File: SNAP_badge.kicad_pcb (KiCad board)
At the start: 2 copper layers, 63.5 x 127 mm, 149 parts, among them P1 MicroB, P2 CONN_01X08, P3 CONN_01X08, P4 CONN_01X10, P5 CONN_01X06, P6 CONN_02X03, Q1 ZXMN2F30FHCT-ND, Q2 Si2305DS, SW1 SWITCH_DPDT, SW2 SW_PUSH, SW3 SW_PUSH, SW4 SW_PUSH, SW5 SW_DIP_8, U1 SM220, U2 AS1115, U3 FT230XS, U4 LD1117S33CTR, U5 LIS3DH, U6 TPS61070, U7 NLSX4373

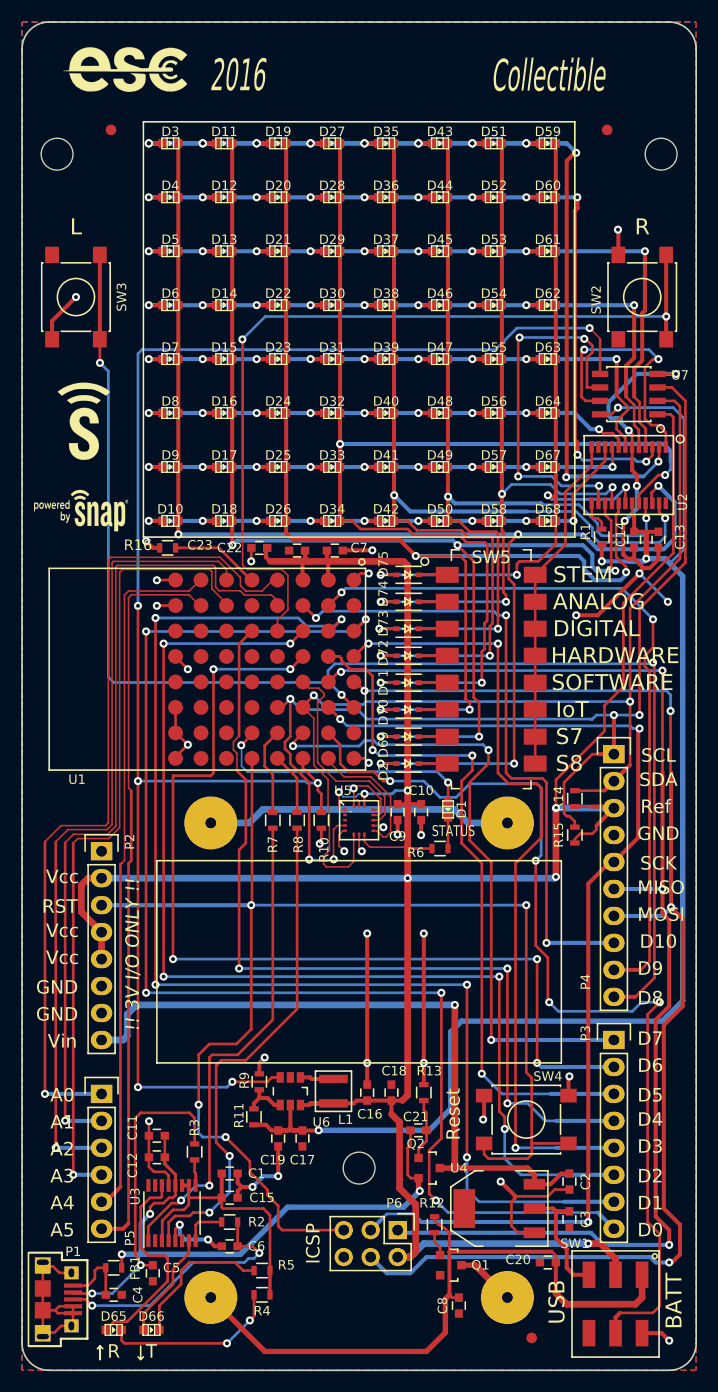
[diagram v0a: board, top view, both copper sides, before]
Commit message: Change to refactored Kicad local libraries
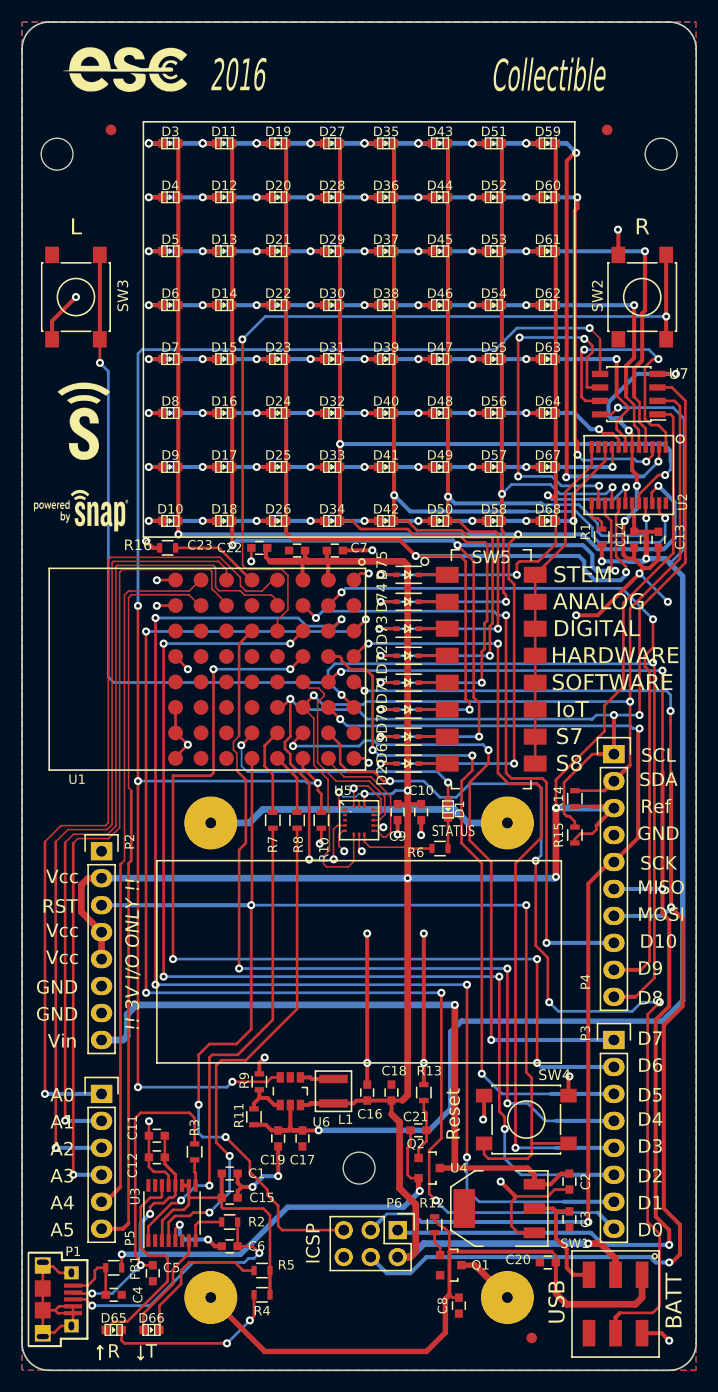
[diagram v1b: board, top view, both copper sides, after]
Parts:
- BT1, BT2: footprint Synapse:BATT_2466 -> Added:BATT_2466
- C1, C18, C2, C21: value 100nF -> 0.1uF
- D1, D10, D11, D12, D13, D14, D15, D16, D17, D18, D19, D20, D21, D22, D23, D24, D25, D26, D27, D28, D29, D3, D30, D31, D32, D33, D34, D35, D36, D37, D38, D39, D4, D40, D41, D42, D43, D44, D45, D46, D47, D48, D49, D5, D50, D51, D52, D53, D54, D55, D56, D57, D58, D59, D6, D60, D61, D62, D63, D64, D65, D66, D67, D68, D7, D8, D9: footprint w_smd_leds:Led_0603 -> Added:Led_0603
- D2, D69, D70, D71, D72, D73, D74, D75: footprint Diodes_SMD:SOD-323 -> Added:SOD-323
- L1: footprint Synapse:TYS-2 -> Added:TYS-2
- P1: footprint Synapse:USBmicroB -> Added:USBmicroB
- SW1: footprint Synapse:SO-DPDT-6 -> Added:SO-DPDT-6
- SW2, SW3, SW4: footprint Buttons_Switches_SMD:SW_SPST_PTS645 -> Added:SW_SPST_PTS645
- SW5: footprint Synapse:DIPSW-16 -> Added:DIPSW-16
- U2: footprint Synapse:QSOP-24 -> Added:QSOP-24
- U5: footprint Synapse:LGA16_3x3 -> Added:LGA16_3x3
- U7: footprint Synapse:SOIC-8_3.9x4.9mm_Pitch1.27mm -> Housings_SOIC:SOIC-8_3.9x4.9mm_Pitch1.27mm
